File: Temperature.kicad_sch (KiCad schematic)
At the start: 15 parts, among them U1 INA283, U2 INA283, U3 INA283

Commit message: ...
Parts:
- removed C15, C6, C8: 0.1u, Capacitor_SMD:C_0603_1608Metric_Pad1.08x0.95mm_HandSolder, symbol Device:C_Small
- removed C16, C7, C9: 56p, Capacitor_SMD:C_0603_1608Metric_Pad1.08x0.95mm_HandSolder, symbol Device:C_Small
- removed R3, R6, R8: 120, Resistor_SMD:R_0603_1608Metric_Pad0.98x0.95mm_HandSolder, symbol Device:R_Small
- removed R4, R5, R7: 0.5m, Resistor_SMD:R_2512_6332Metric_Pad1.40x3.35mm_HandSolder, symbol Device:R
- removed U1, U2, U3: INA283, Package_SO:SOIC-8_3.9x4.9mm_P1.27mm, symbol Amplifier_Current:INA283
- added C10, C11, C12: 1u, Capacitor_SMD:C_0603_1608Metric_Pad1.08x0.95mm_HandSolder, symbol Device:C_Small
- added C13, C14, C17: 100n, Capacitor_SMD:C_0603_1608Metric_Pad1.08x0.95mm_HandSolder, symbol Device:C_Small
- added C18: 0.1u, Capacitor_SMD:C_0603_1608Metric_Pad1.08x0.95mm_HandSolder, symbol Device:C_Small
- added R10, R11, R9: 15k, Resistor_SMD:R_0603_1608Metric_Pad0.98x0.95mm_HandSolder, symbol Device:R_Small
- added R12, R13, R14: 1k, Resistor_SMD:R_0603_1608Metric_Pad0.98x0.95mm_HandSolder, symbol Device:R_Small
- added R15, R16, R17: 9.1k, Resistor_SMD:R_0603_1608Metric_Pad0.98x0.95mm_HandSolder, symbol Device:R_Small
- added R18, R19, R20: 120, Resistor_SMD:R_0603_1608Metric_Pad0.98x0.95mm_HandSolder, symbol Device:R_Small
- added U4: LMV324, Package_SO:SOIC-14_3.9x8.7mm_P1.27mm, symbol Amplifier_Operational:LMV324
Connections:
- new net: R13.2, R16.1, U4.6 (-)
- new net: R15.2, R18.2, U4.1
- new net: R14.2, R17.1, U4.9 (-)
- new net: R16.2, R19.2, U4.7
- new net: R17.2, R20.2, U4.8
- new net: R12.2, R15.1, U4.2 (-)
- new net +3.3VA: C18.1, R10.1, R11.1, R9.1, U4.4 (V+)
- new net GNDA: C10.2, C11.2, C12.2, C13.2, C14.2, C17.2, C18.2, R12.1, R13.1, R14.1, U4.11 (V-)
- new net PTC_Coil_A: C10.1, R9.2, U4.3 (+)
- new net PTC_Coil_B: C11.1, R10.2, U4.5 (+)
- new net PTC_Coil_C: C12.1, R11.2, U4.10 (+)
- new net Temp_Coil_A_MCU: C13.1, R18.1
- new net Temp_Coil_B_MCU: C14.1, R19.1
- new net Temp_Coil_C_MCU: C17.1, R20.1
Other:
- note added: "Питание ОУ"
- note added: "Температура обмотки B"
- note added: "Температура обмотки А"
- note added: "Температура обмотки С"
- note removed: "Измерение тока А"
- note removed: "Измерение тока В"
- note removed: "Измерение тока С"

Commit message: VER2.0
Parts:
- removed C12: 1u, Capacitor_SMD:C_0603_1608Metric_Pad1.08x0.95mm_HandSolder, symbol Device:C_Small
- removed C17: 100n, Capacitor_SMD:C_0603_1608Metric_Pad1.08x0.95mm_HandSolder, symbol Device:C_Small
- removed R11: 15k, Resistor_SMD:R_0603_1608Metric_Pad0.98x0.95mm_HandSolder, symbol Device:R_Small
- removed R14: 1k, Resistor_SMD:R_0603_1608Metric_Pad0.98x0.95mm_HandSolder, symbol Device:R_Small
- removed R17: 9.1k, Resistor_SMD:R_0603_1608Metric_Pad0.98x0.95mm_HandSolder, symbol Device:R_Small
- removed R20: 120, Resistor_SMD:R_0603_1608Metric_Pad0.98x0.95mm_HandSolder, symbol Device:R_Small
- removed unit 3 of U4
- added U4 (x2): LMV324, Package_SO:SOIC-14_3.9x8.7mm_P1.27mm, symbol Amplifier_Operational:LMV324
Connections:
- no-connect marks 0 -> 6
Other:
- note removed: "Температура обмотки С"

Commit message: Убрал лишние шунты
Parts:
- renumbered C13 to C11, C11 to C12, C14 to C13, R18 to R10, R10 to R11, R19 to R12, R16 to R15, R13 to R16, R12 to R18, R15 to R19

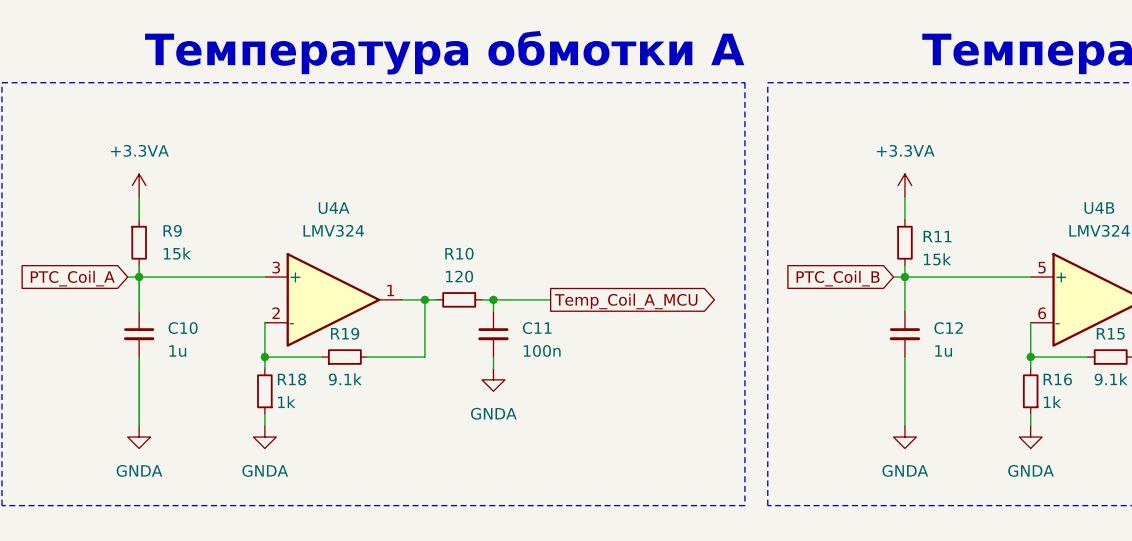
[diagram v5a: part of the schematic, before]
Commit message: Изменил резисторы подтяжки для PTC
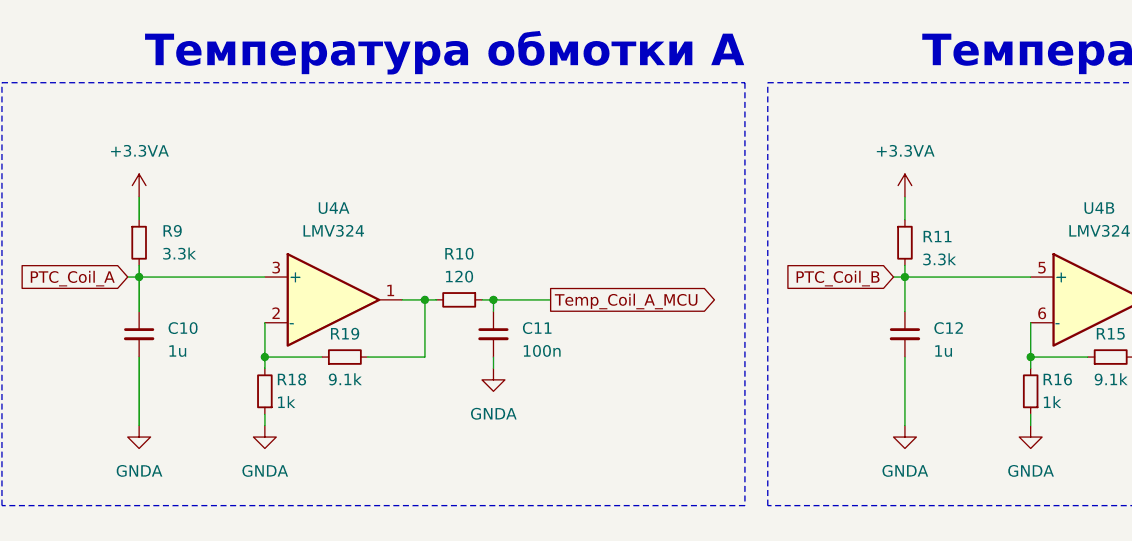
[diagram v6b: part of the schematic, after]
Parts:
- R11, R9: value 15k -> 3.3k
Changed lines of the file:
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@@
 			)
 		)
-		(property "Value" "15k"
+		(property "Value" "3.3k"
 			(at 132.08 66.0399 0)
 			(effects
@@
 			)
 		)
-		(property "Value" "15k"
+		(property "Value" "3.3k"
 			(at 47.625 65.405 0)
 			(effects
